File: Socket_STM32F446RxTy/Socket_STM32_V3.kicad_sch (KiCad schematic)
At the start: 68 parts, among them P1 PAD_CASTELLATED_HOLE_CORNER, P10 PAD_1_1.51.2, P11 PAD_1_1.51.2, P12 PAD_1_1.51.2, P13 PAD_1_1.51.2, P14 PAD_CASTELLATED_HOLE_CORNER, P15 PAD_1_1.51.2, P16 PAD_1_1.51.2, P17 PAD_1_1.51.2, P18 PAD_1_1.51.2, P19 PAD_1_1.51.2, P2 PAD_1_1.51.2, P20 PAD_1_1.51.2, P21 PAD_1_1.51.2, P22 PAD_1_1.51.2, P23 PAD_1_1.51.2, P24 PAD_1_1.51.2, P25 PAD_1_1.51.2, P26 PAD_1_1.51.2, P27 PAD_CASTELLATED_HOLE_CORNER, P28 PAD_1_1.51.2, P29 PAD_1_1.51.2, P3 PAD_1_1.51.2, P30 PAD_1_1.51.2, P31 PAD_1_1.51.2, P32 PAD_1_1.51.2, P33 PAD_1_1.51.2, P34 PAD_1_1.51.2, P35 PAD_1_1.51.2, P36 PAD_1_1.51.2, P37 PAD_1_1.51.2, P38 PAD_1_1.51.2, P39 PAD_1_1.51.2, P4 PAD_1_1.51.2, P40 PAD_CASTELLATED_HOLE_CORNER, P41 PAD_1_1.51.2, P42 PAD_1_1.51.2, P43 PAD_1_1.51.2, P44 PAD_1_1.51.2, P45 PAD_1_1.51.2, P46 PAD_1_1.51.2, P47 PAD_1_1.51.2, P48 PAD_1_1.51.2, P49 PAD_1_1.51.2, P5 PAD_1_1.51.2, P50 PAD_1_1.51.2, P51 PAD_1_1.51.2, P52 PAD_1_1.51.2, P53 GH, P6 PAD_1_1.51.2, P7 PAD_1_1.51.2, P8 PAD_1_1.51.2, P9 PAD_1_1.51.2, U10 STM32F446RET6, X10 16MHz

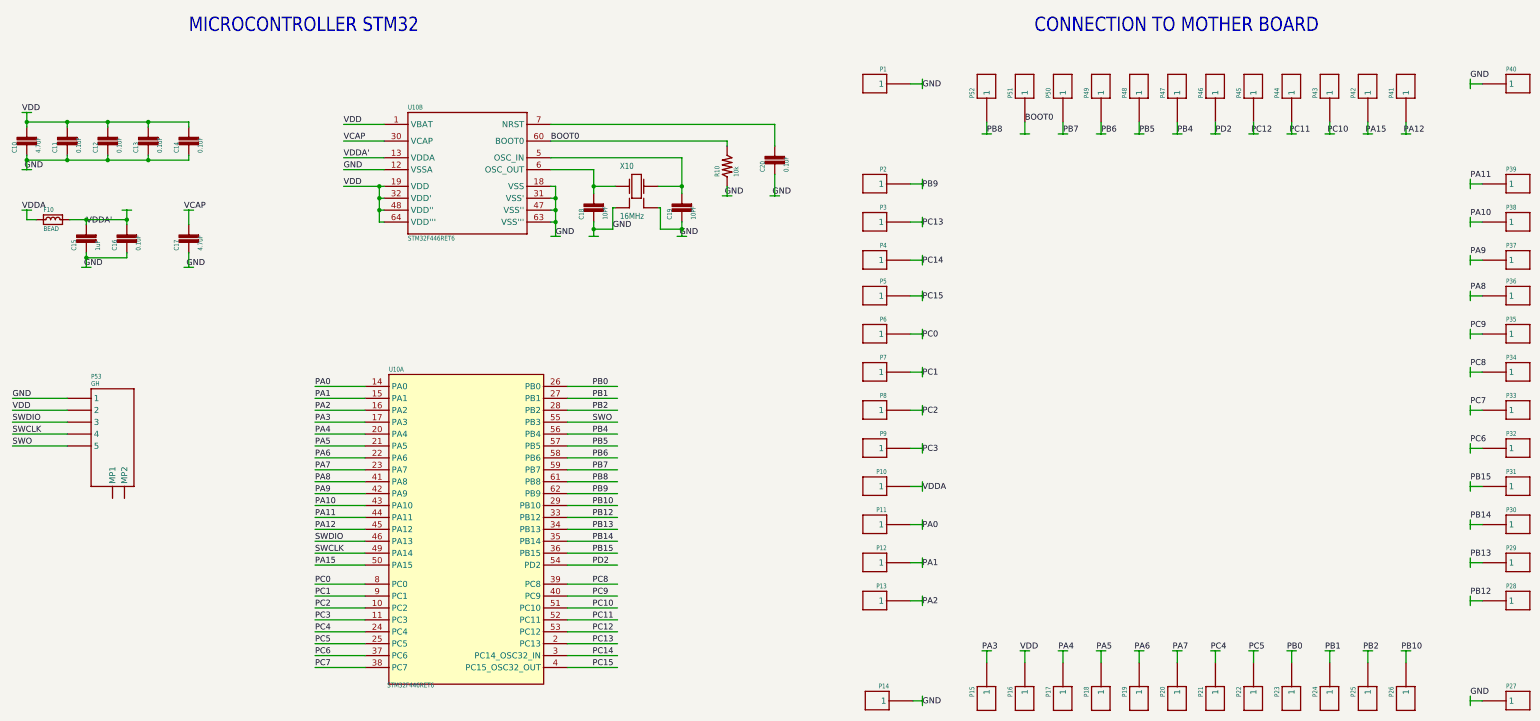
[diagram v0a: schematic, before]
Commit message: Update symbols & schematic
* Improve symbols in library
* Update all symbols in schematic from library
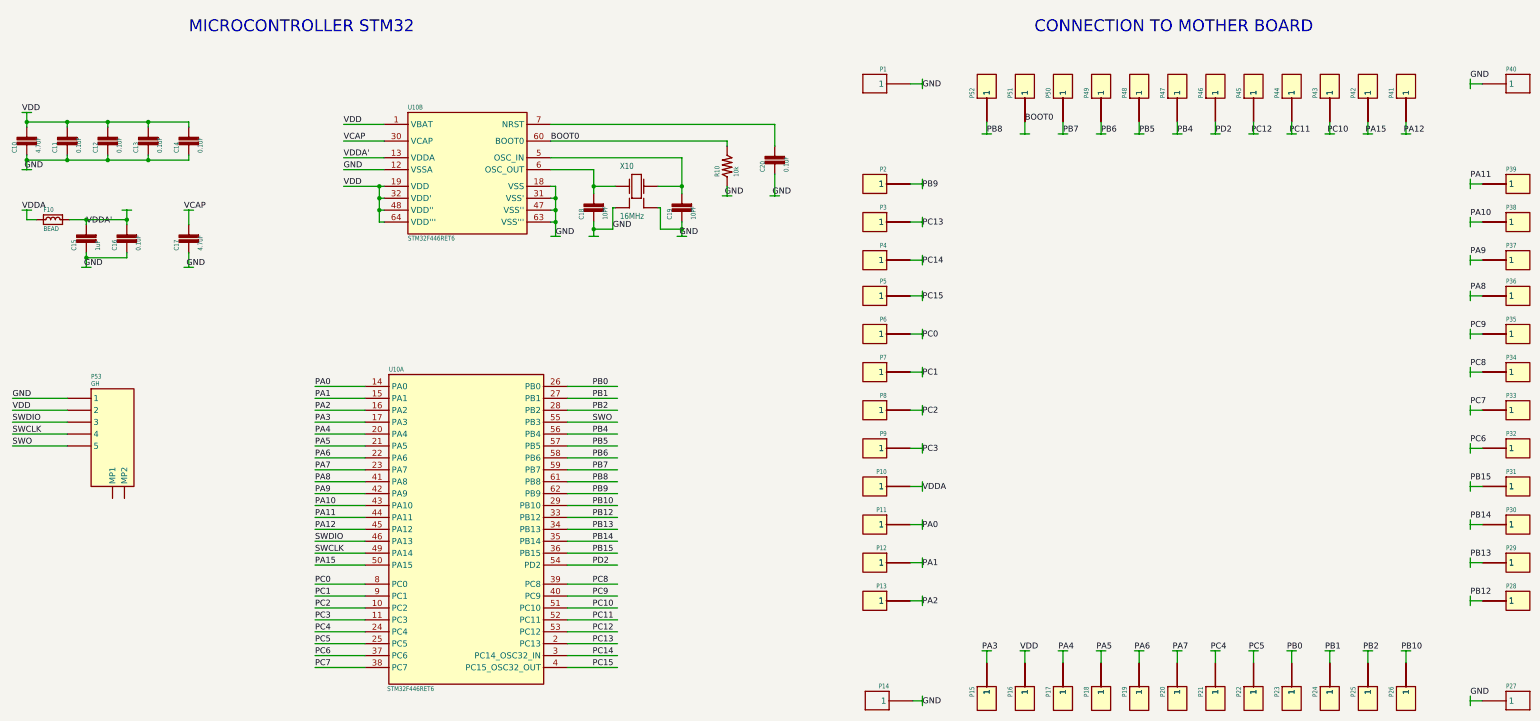
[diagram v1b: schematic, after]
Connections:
- net BOOT0: no longer P51.1
- net PA0: no longer P11.1
- net PA1: no longer P12.1
- net PA10: no longer P38.1
- net PA11: no longer P39.1
- net PA12: no longer P41.1
- net PA15: no longer P42.1
- net PA2: no longer P13.1
- net PA3: no longer P15.1
- net PA4: no longer P17.1
- net PA5: no longer P18.1
- net PA6: no longer P19.1
- net PA7: no longer P20.1
- net PA8: no longer P36.1
- net PA9: no longer P37.1
- net PB0: no longer P23.1
- net PB1: no longer P24.1
- net PB10: no longer P26.1
- net PB12: no longer P28.1
- net PB13: no longer P29.1
- net PB14: no longer P30.1
- net PB15: no longer P31.1
- net PB2: no longer P25.1
- net PB4: no longer P47.1
- net PB5: no longer P48.1
- net PB6: no longer P49.1
- net PB7: no longer P50.1
- net PB8: no longer P52.1
- net PB9: no longer P2.1
- net PC0: no longer P6.1
- net PC1: no longer P7.1
- net PC10: no longer P43.1
- net PC11: no longer P44.1
- net PC12: no longer P45.1
- net PC13: no longer P3.1
- net PC14: no longer P4.1
- net PC15: no longer P5.1
- net PC2: no longer P8.1
- net PC3: no longer P9.1
- net PC4: no longer P21.1
- net PC5: no longer P22.1
- net PC6: no longer P32.1
- net PC7: no longer P33.1
- net PC8: no longer P34.1
- net PC9: no longer P35.1
- net PD2: no longer P46.1
- net VDD: no longer P16.1
- net VDDA: no longer P10.1
